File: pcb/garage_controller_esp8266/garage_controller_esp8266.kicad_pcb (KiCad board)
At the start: 2 copper layers, 100 x 100 mm, 38 parts, among them J1 Connections, J2 Conn_01x03_Socket, Q1 2N7002, Q2 2N7002, Q3 2N7002, U1 Wemos D1 mini connector, U2 MCP23017_SO

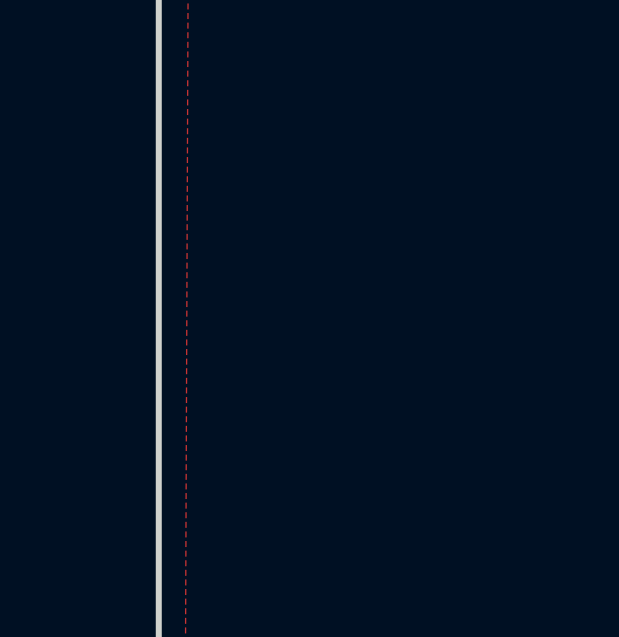
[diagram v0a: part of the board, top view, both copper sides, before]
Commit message: Changed pins for buttons and added clipper
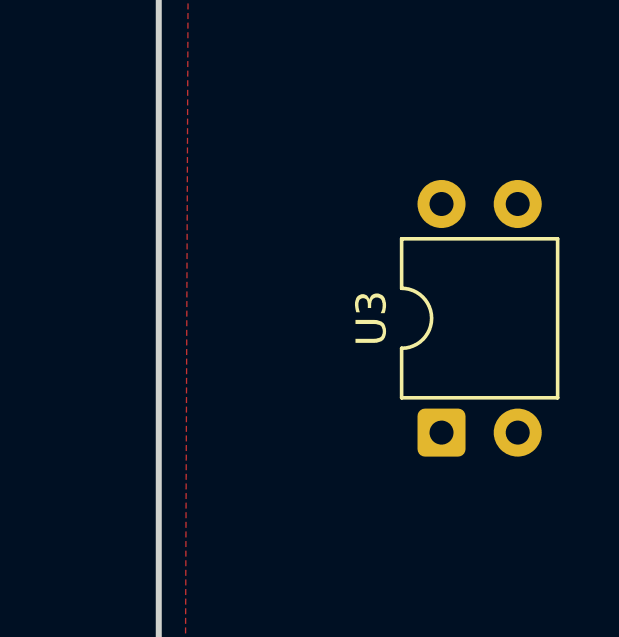
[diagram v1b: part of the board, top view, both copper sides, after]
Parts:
- added U3: LTV-817, Package_DIP:DIP-4_W7.62mm, F.Cu at (159.4, 95.3)
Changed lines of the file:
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@@
 	(net 52 "Net-(D2-A)")
 	(net 53 "unconnected-(D4-K-Pad2)")
+	(net 54 "unconnected-(U3-Pad1)")
+	(net 55 "unconnected-(U3-Pad3)")
+	(net 56 "unconnected-(U3-Pad4)")
+	(net 57 "unconnected-(U3-Pad2)")
 	(footprint "Resistor_SMD:R_0805_2012Metric_Pad1.20x1.40mm_HandSolder"
 		(layer "F.Cu")
@@
 			(offset
 				(xyz 0 0 0)
+			)
+			(scale
+				(xyz 1 1 1)
+			)
+			(rotate
+				(xyz 0 0 0)
+			)
+		)
+	)
+	(footprint "Package_DIP:DIP-4_W7.62mm"
+		(layer "F.Cu")
+		(at 159.425 95.305 90)
+		(descr "4-lead though-hole mounted DIP package, row spacing 7.62mm (300 mils)")
+		(tags "THT DIP DIL PDIP 2.54mm 7.62mm 300mil")
+		(property "Reference" "U3"
+			(at 3.81 -2.33 90)
+			(layer "F.SilkS")
+			(effects
+				(font
+					(size 1 1)
+					(thickness 0.15)
+				)
+			)
+		)
+		(property "Value" "LTV-817"
+			(at 3.81 4.87 90)
+			(layer "F.Fab")
+			(effects
+				(font
+					(size 1 1)
+					(thickness 0.15)
+				)
+			)
+		)
+		(property "Datasheet" "http://www.us.liteon.com/downloads/LTV-817-827-847.PDF"
+			(at 0 0 90)
+			(layer "F.Fab")
+			(hide yes)
+			(effects
+				(font
+					(size 1.27 1.27)
+					(thickness 0.15)
+				)
+			)
+		)
+		(property "Description" "DC Optocoupler, Vce 35V, CTR 50%, DIP-4"
+			(at 0 0 90)
+			(layer "F.Fab")
+			(hide yes)
+			(effects
+				(font
+					(size 1.27 1.27)
+					(thickness 0.15)
+				)
+			)
+		)
+		(property ki_fp_filters "DIP*W7.62mm*")
+		(sheetname "/")
+		(sheetfile "garage_controller_esp8266.kicad_sch")
+		(attr through_hole)
+		(fp_line
+			(start 6.46 -1.33)
+			(end 4.81 -1.33)
+			(stroke
+				(width 0.12)
+				(type solid)
+			)
+			(layer "F.SilkS")
+		)
+		(fp_line
+			(start 2.81 -1.33)
+			(end 1.16 -1.33)
+			(stroke
+				(width 0.12)
+				(type solid)
+			)
+			(layer "F.SilkS")
+		)
+		(fp_line
+			(start 1.16 -1.33)
+			(end 1.16 3.87)
+			(stroke
+				(width 0.12)
+				(type solid)
+			)
+			(layer "F.SilkS")
+		)
+		(fp_line
+			(start 6.46 3.87)
+			(end 6.46 -1.33)
+			(stroke
+				(width 0.12)
+				(type solid)
+			)
+			(layer "F.SilkS")
+		)
+		(fp_line
+			(start 1.16 3.87)
+			(end 6.46 3.87)
+			(stroke
+				(width 0.12)
+				(type solid)
+			)
+			(layer "F.SilkS")
+		)
+		(fp_arc
+			(start 4.81 -1.33)
+			(mid 3.81 -0.33)
+			(end 2.81 -1.33)
+			(stroke
+				(width 0.12)
+				(type solid)
+			)
+			(layer "F.SilkS")
+		)
+		(fp_rect
+			(start -1.06 -1.52)
+			(end 8.67 4.07)
+			(stroke
+				(width 0.05)
+				(type solid)
+			)
+			(fill no)
+			(layer "F.CrtYd")
+		)
+		(fp_line
+			(start 6.985 -1.27)
+			(end 6.985 3.81)
+			(stroke
+				(width 0.1)
+				(type solid)
+			)
+			(layer "F.Fab")
+		)
+		(fp_line
+			(start 1.635 -1.27)
+			(end 6.985 -1.27)
+			(stroke
+				(width 0.1)
+				(type solid)
+			)
+			(layer "F.Fab")
+		)
+		(fp_line
+			(start 0.635 -0.27)
+			(end 1.635 -1.27)
+			(stroke
+				(width 0.1)
+				(type solid)
+			)
+			(layer "F.Fab")
+		)
+		(fp_line
+			(start 6.985 3.81)
+			(end 0.635 3.81)
+			(stroke
+				(width 0.1)
+				(type solid)
+			)
+			(layer "F.Fab")
+		)
+		(fp_line
+			(start 0.635 3.81)
+			(end 0.635 -0.27)
+			(stroke
+				(width 0.1)
+				(type solid)
+			)
+			(layer "F.Fab")
+		)
+		(fp_text user "${REFERENCE}"
+			(at 3.81 1.27 90)
+			(layer "F.Fab")
+			(effects
+				(font
+					(size 1 1)
+					(thickness 0.15)
+				)
+			)
+		)
+		(pad "1" thru_hole roundrect
+			(at 0 0 90)
+			(size 1.6 1.6)
+			(drill 0.8)
+			(layers "*.Cu" "*.Mask")
+			(remove_unused_layers no)
+			(roundrect_rratio 0.15625)
+			(net 54 "unconnected-(U3-Pad1)")
+			(pintype "passive")
+		)
+		(pad "2" thru_hole circle
+			(at 0 2.54 90)
+			(size 1.6 1.6)
+			(drill 0.8)
+			(layers "*.Cu" "*.Mask")
+			(remove_unused_layers no)
+			(net 57 "unconnected-(U3-Pad2)")
+			(pintype "passive")
+		)
+		(pad "3" thru_hole circle
+			(at 7.62 2.54 90)
+			(size 1.6 1.6)
+			(drill 0.8)
+			(layers "*.Cu" "*.Mask")
+			(remove_unused_layers no)
+			(net 55 "unconnected-(U3-Pad3)")
+			(pintype "passive")
+		)
+		(pad "4" thru_hole circle
+			(at 7.62 0 90)
+			(size 1.6 1.6)
+			(drill 0.8)
+			(layers "*.Cu" "*.Mask")
+			(remove_unused_layers no)
+			(net 56 "unconnected-(U3-Pad4)")
+			(pintype "passive")
+		)
+		(embedded_fonts no)
+		(model "${KICAD9_3DMODEL_DIR}/Package_DIP.3dshapes/DIP-4_W7.62mm.step"
+			(offset
+				(xyz 0 0 0)
